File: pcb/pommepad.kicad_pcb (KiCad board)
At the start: 2 copper layers, 95 x 90 mm, 28 parts, among them SW1 SW_Push, SW2 SW_Push, SW3 SW_Push, SW4 SW_Push, SW5 SW_Push, SW6 SW_Push, U1 XIAO-RP2040-DIP, U2 OLED_0.91_128x32

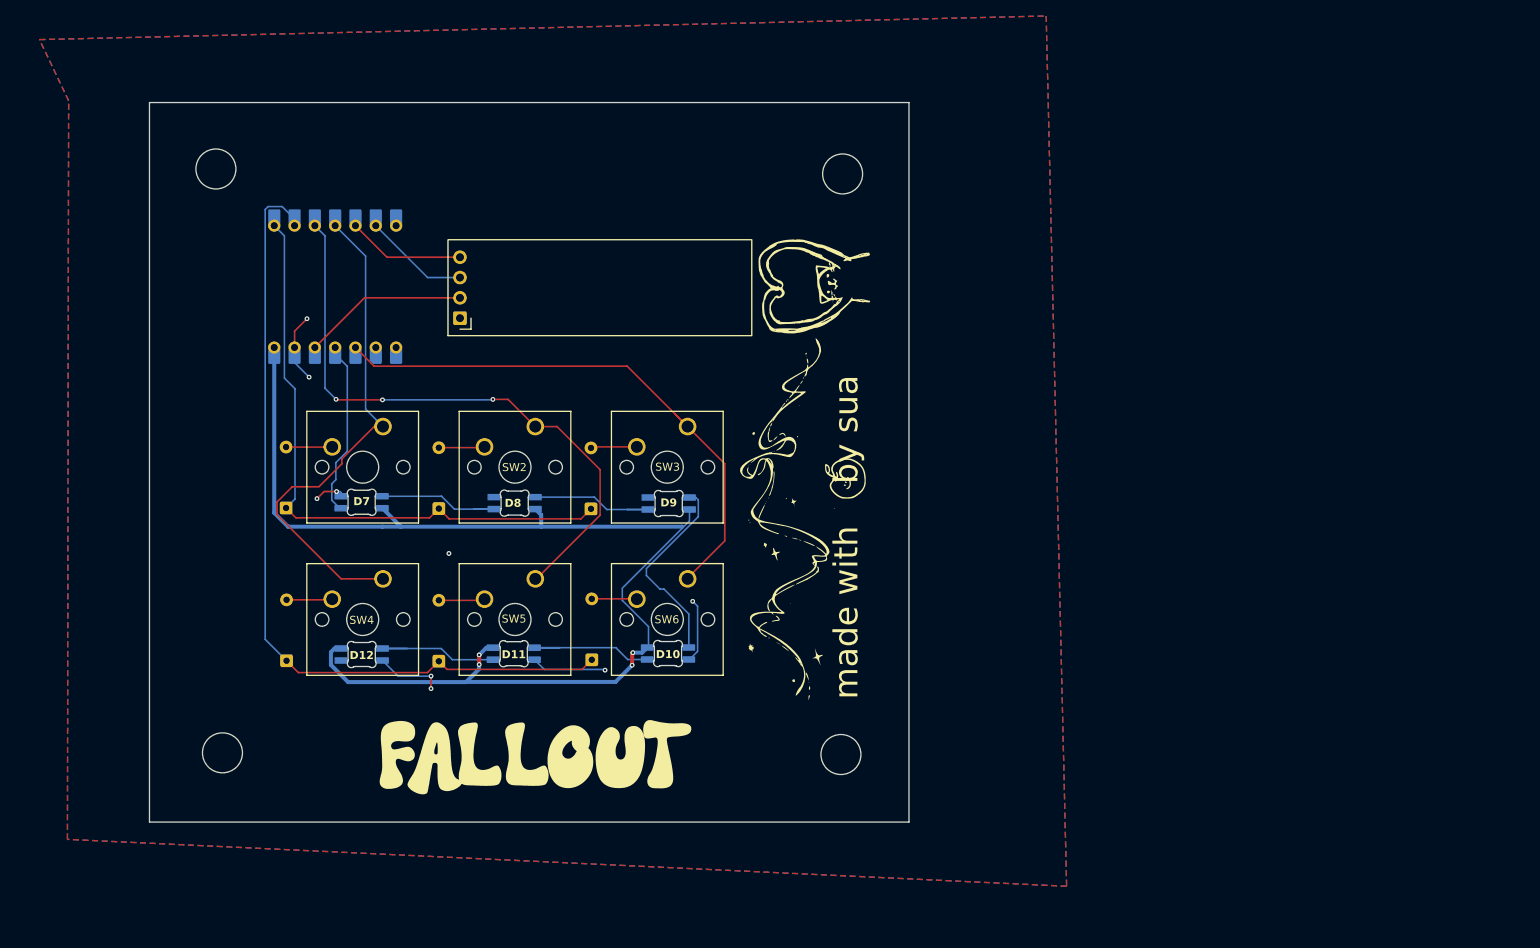
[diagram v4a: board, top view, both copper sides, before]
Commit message: OOOPSSS
moved rp2040 to the edge I FORGOT ABOUT THAT UHAUSDHUASH
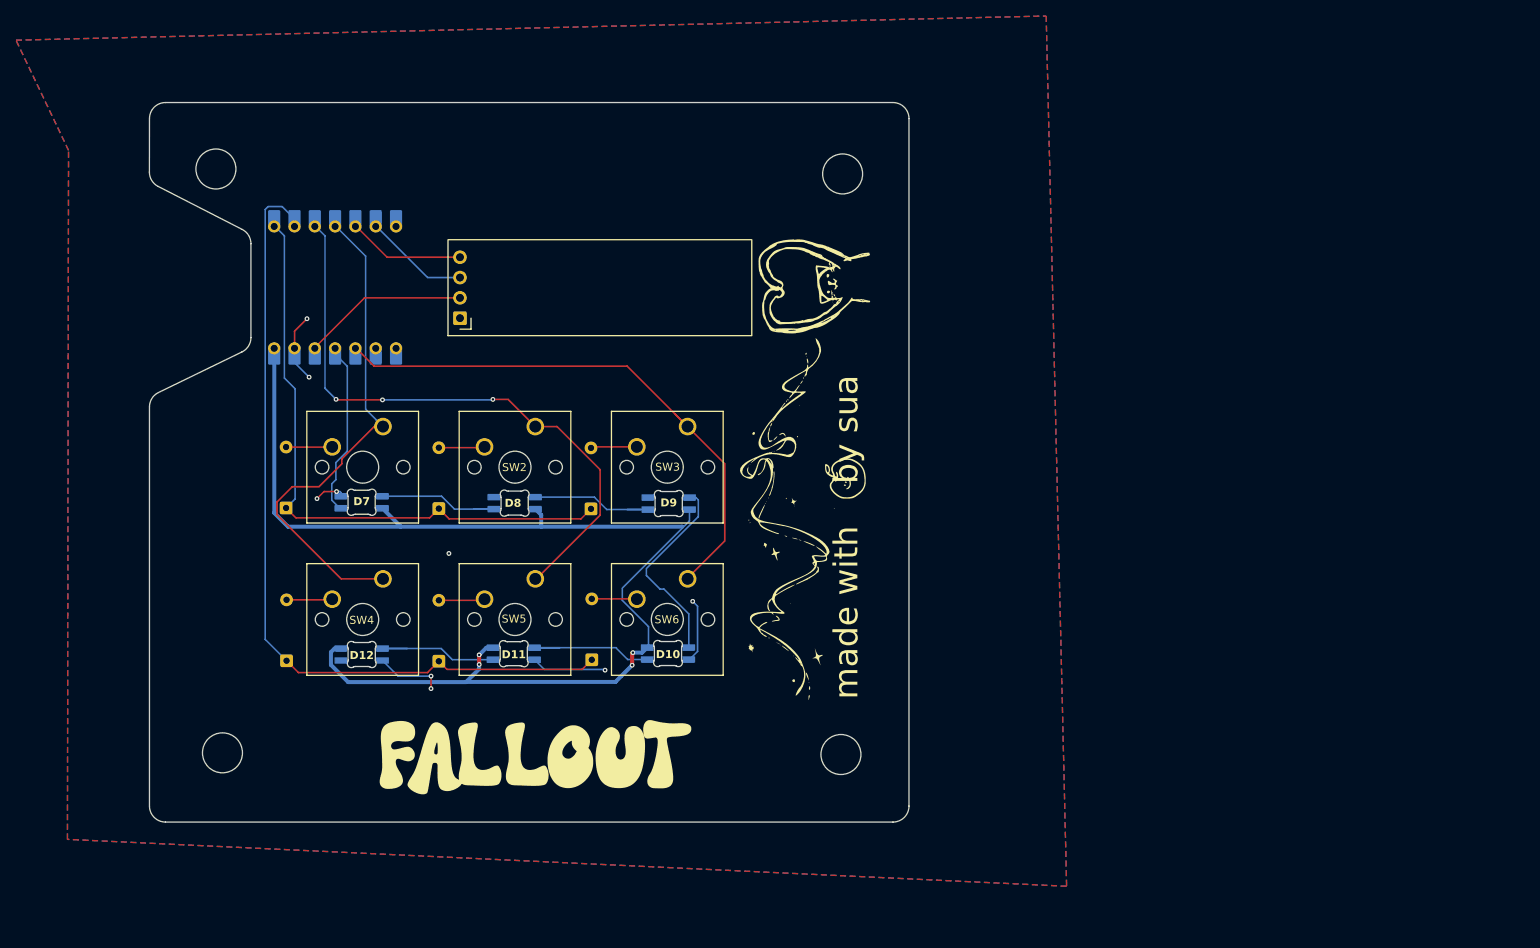
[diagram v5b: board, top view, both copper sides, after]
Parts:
- moved G*** 38.5 mm to (68.0, 70.4)
- moved U1 0.10 mm to (63.8, 63.9)
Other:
- outline, holes or cut-outs redrawn
- board text added: "SOUP IS BANNED"

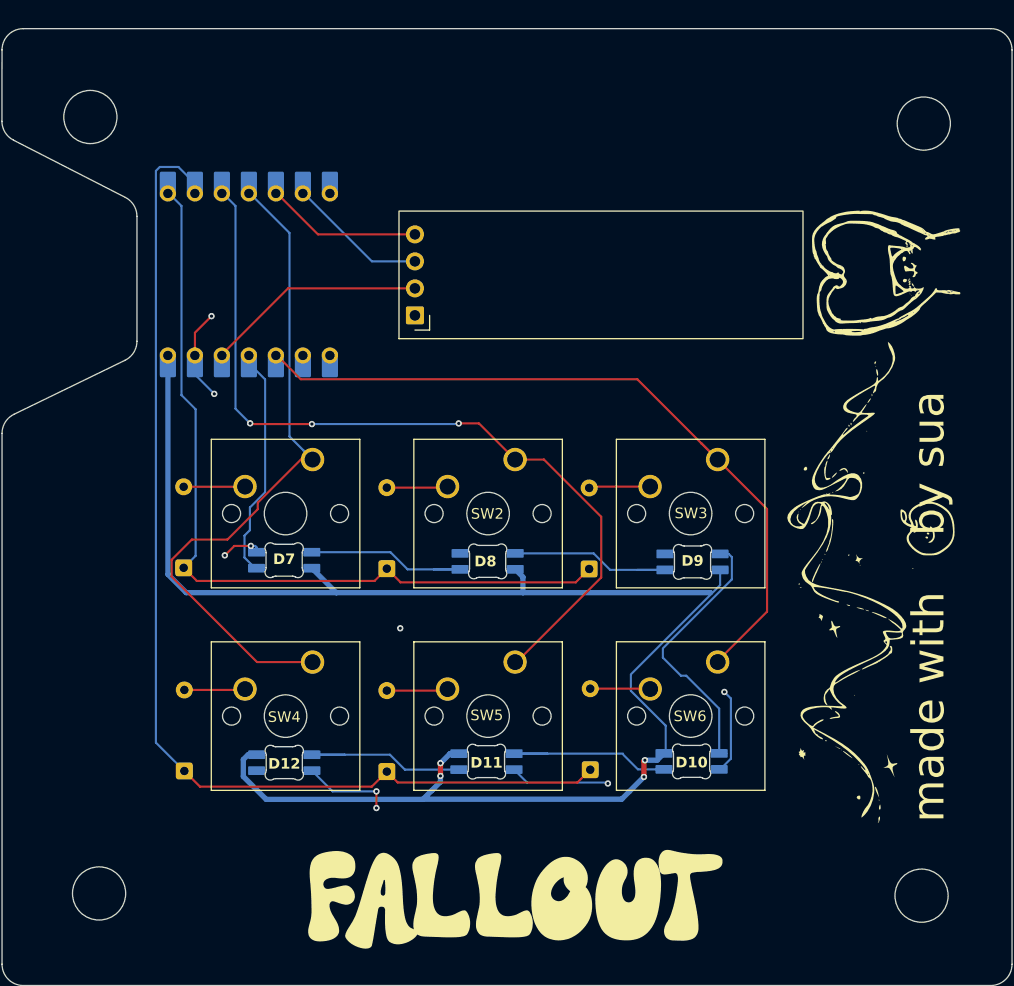
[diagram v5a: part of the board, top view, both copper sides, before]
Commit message: CHANGING IT BACK
run it back we using m3 instead why did moronic eason peng tell me to use 5mm
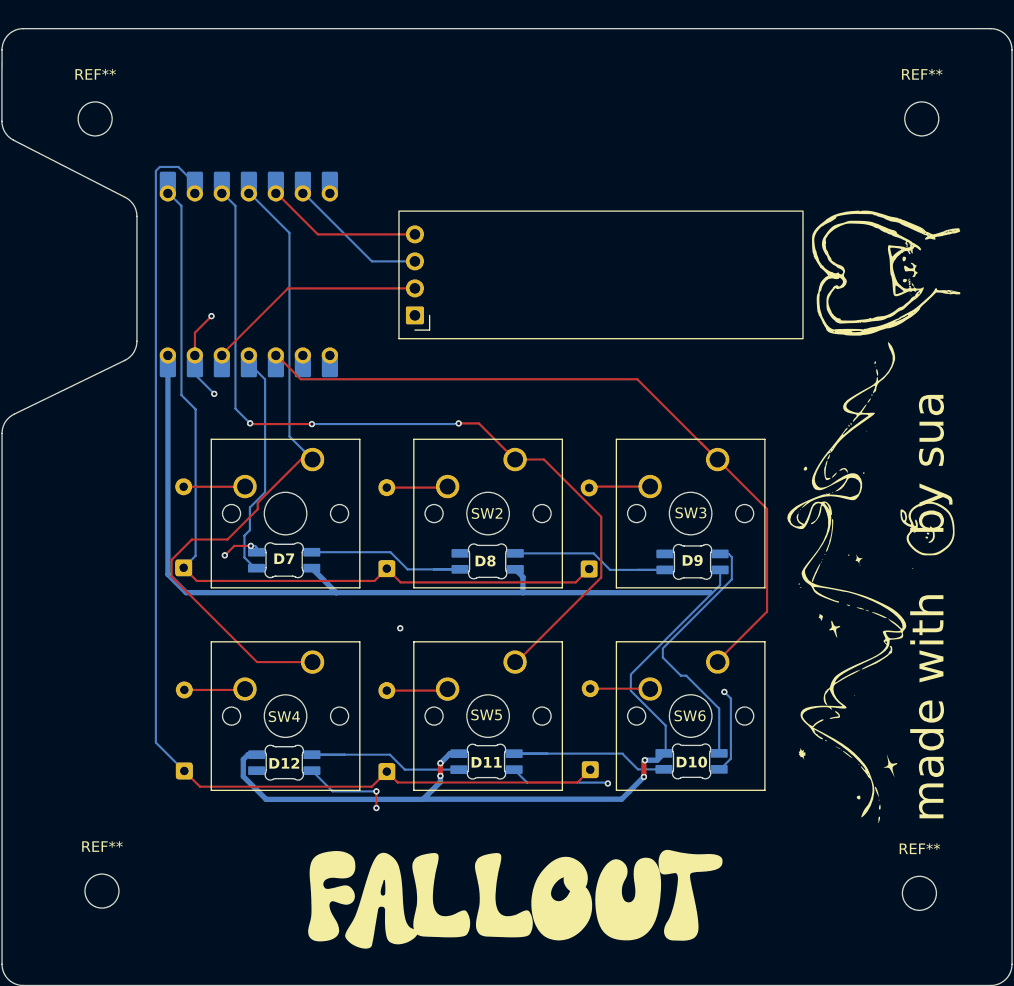
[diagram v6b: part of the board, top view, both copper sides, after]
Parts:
- removed the REF** at (127.1, 122.3)
- removed the REF** at (49.8, 122.1)
- removed the REF** at (127.3, 49.7)
- removed the REF** at (48.9, 49.1)
- added REF**: MountingHole_3.2mm_M3, MountingHole:MountingHole_3.2mm_M3, F.Cu at (49.4, 49.2)
- added REF**: MountingHole_3.2mm_M3, MountingHole:MountingHole_3.2mm_M3, F.Cu at (127.1, 49.2)
- added REF**: MountingHole_3.2mm_M3, MountingHole:MountingHole_3.2mm_M3, F.Cu at (126.9, 122.1)
- added REF**: MountingHole_3.2mm_M3, MountingHole:MountingHole_3.2mm_M3, F.Cu at (50.0, 121.9)
